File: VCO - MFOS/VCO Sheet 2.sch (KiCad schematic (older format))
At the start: 63 parts, among them J10 PWM_CV, J11 SQU, J18 RV10P3, J19 RV10P1, J20 RV10P2, J21 GND_CONN, J22 +12V_CONN, J23 -12V_CONN, J7 RMP, J8 TRI, J9 SIN, U3 TL074, U4 LM13700, U5 TL072, U6 TL071

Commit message: whoops
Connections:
- net Earth: now also R32.2, U4.4 (-)
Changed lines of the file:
@@
 Connection ~ 9850 5500
 Connection ~ 9850 5600
+$Comp
+L power:Earth #PWR?
+U 1 1 5FF7FD6C
+P 3400 6650
+F 0 "#PWR?" H 3400 6400 50  0001 C CNN
+F 1 "Earth" H 3400 6500 50  0001 C CNN
+F 2 "" H 3400 6650 50  0001 C CNN
+F 3 "~" H 3400 6650 50  0001 C CNN
+	1    3400 6650
+	1    0    0    -1
+$EndComp
+Wire Wire Line
+	3400 6650 3400 6600
+Connection ~ 3400 6600
 $EndSCHEMATC

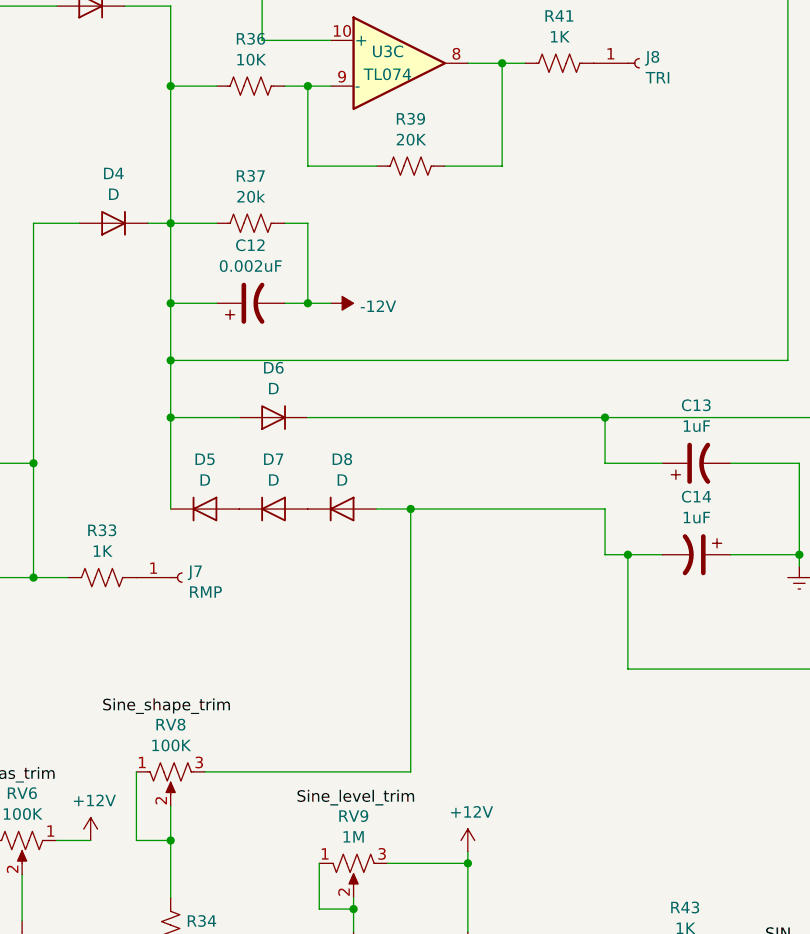
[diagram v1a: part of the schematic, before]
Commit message: fixed error and rerouted VCO
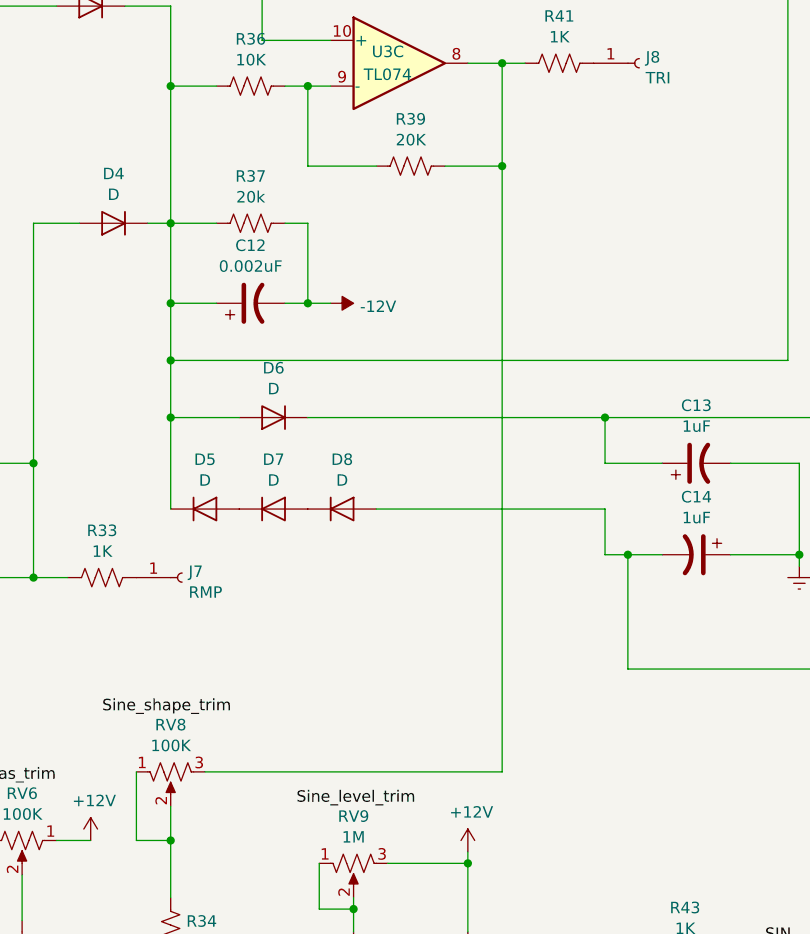
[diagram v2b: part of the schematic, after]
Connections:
- net at R39.2, R41.2, U3.8: now also RV8.3
- net at C14.2, D8.2 (A), U5.5 (+): no longer RV8.3
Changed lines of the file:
@@
 	5650 3750 5900 3750
-Wire Wire Line
-	4650 3950 4800 3950
 Wire Wire Line
 	5650 3950 5650 4150
@@
 Wire Wire Line
 	3750 5400 3750 5250
-Wire Wire Line
-	3900 5100 4800 5100
-Wire Wire Line
-	4800 5100 4800 3950
-Connection ~ 4800 3950
-Wire Wire Line
-	4800 3950 5650 3950
 Wire Wire Line
 	4550 5800 4550 5700
@@
 	3400 6650 3400 6600
 Connection ~ 3400 6600
+Wire Wire Line
+	4650 3950 5650 3950
+Wire Wire Line
+	5200 2450 5200 5100
+Wire Wire Line
+	3900 5100 5200 5100
+Connection ~ 5200 2450
 $EndSCHEMATC
